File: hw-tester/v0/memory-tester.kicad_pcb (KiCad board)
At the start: 2 copper layers, 32 x 51 mm, 7 parts, among them J1 Conn_01x08, J2 Conn_02x14_Odd_Even, U2 74HCT595, U3 74HCT595, U4 74HCT595, U5 74HCT595, U6 74LS597

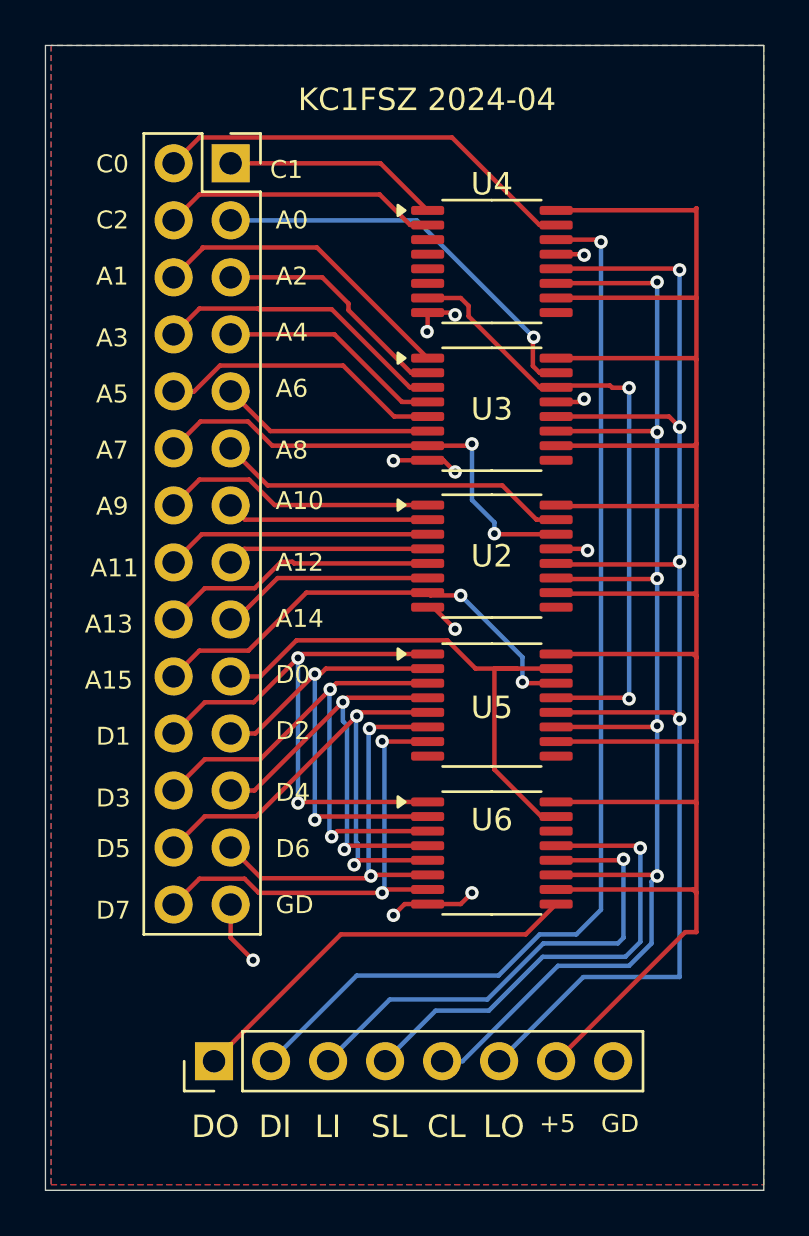
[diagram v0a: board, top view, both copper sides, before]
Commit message: Cleaned up a HW bug in the tester, provided docs
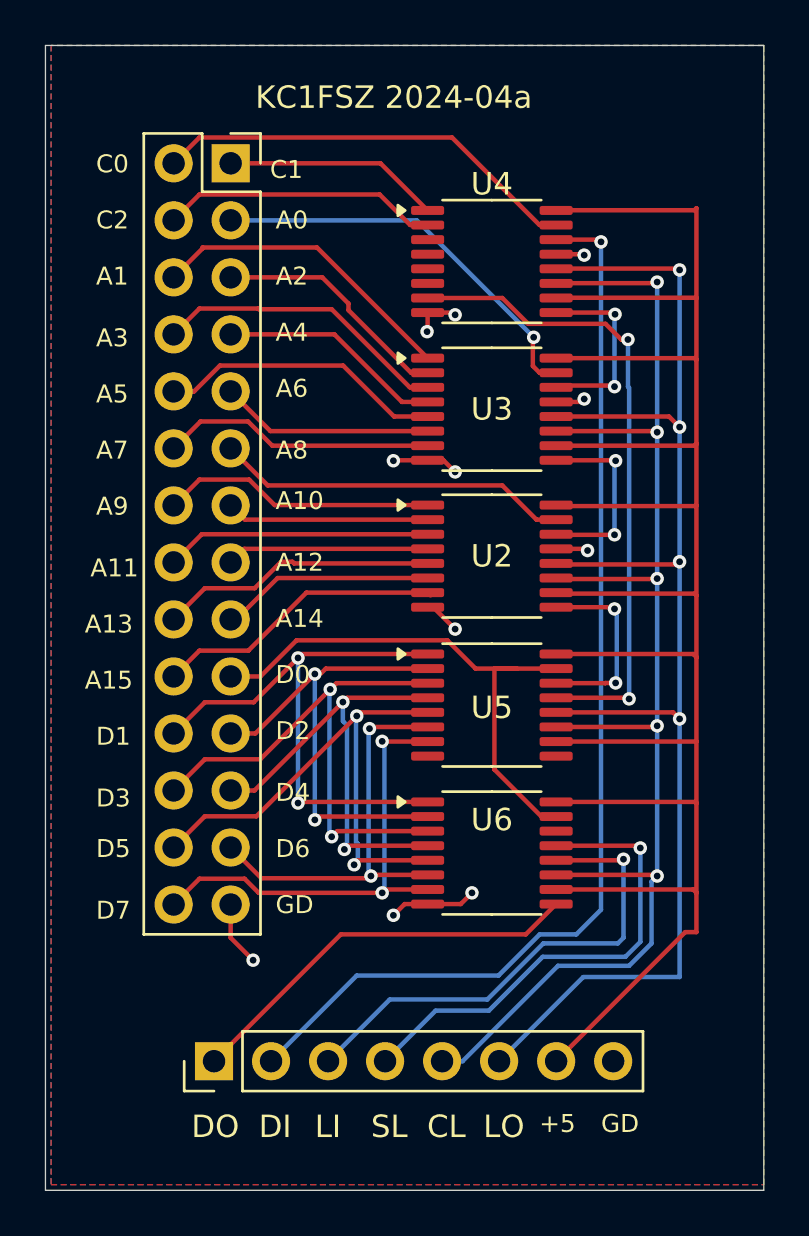
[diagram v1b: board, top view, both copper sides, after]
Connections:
- U2 pad 14: A7 -> CHAIN1
- U2 pad 9: unconnected-(U2-QH'-Pad9) -> CHAIN2
- U3 pad 14: C7 -> CHAIN0
- U3 pad 9: unconnected-(U3-QH'-Pad9) -> CHAIN1
- U4 pad 9: unconnected-(U4-QH'-Pad9) -> CHAIN0
- U5 pad 14: A15 -> CHAIN2
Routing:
- net A7: track 21.4 -> 12.3 mm, vias 2 -> 0
- net CHAIN2: track 0.00 -> 8.65 mm, vias 0 -> 2
- net CHAIN0: track 0.00 -> 8.54 mm, vias 0 -> 2
- net CHAIN1: track 0.00 -> 8.20 mm, vias 0 -> 2
- net A15: track 20.9 -> 13.0 mm, vias 2 -> 0
- net C7: track 28.1 -> 29.0 mm
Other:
- board text added: "KC1FSZ 2024-04a"
- board text removed: "KC1FSZ 2024-04"
